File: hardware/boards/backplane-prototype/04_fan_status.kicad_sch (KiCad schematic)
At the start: 20 parts, among them J9 12V 3-WIRE FAN, Q1 AO3407A, Q2 2N7002

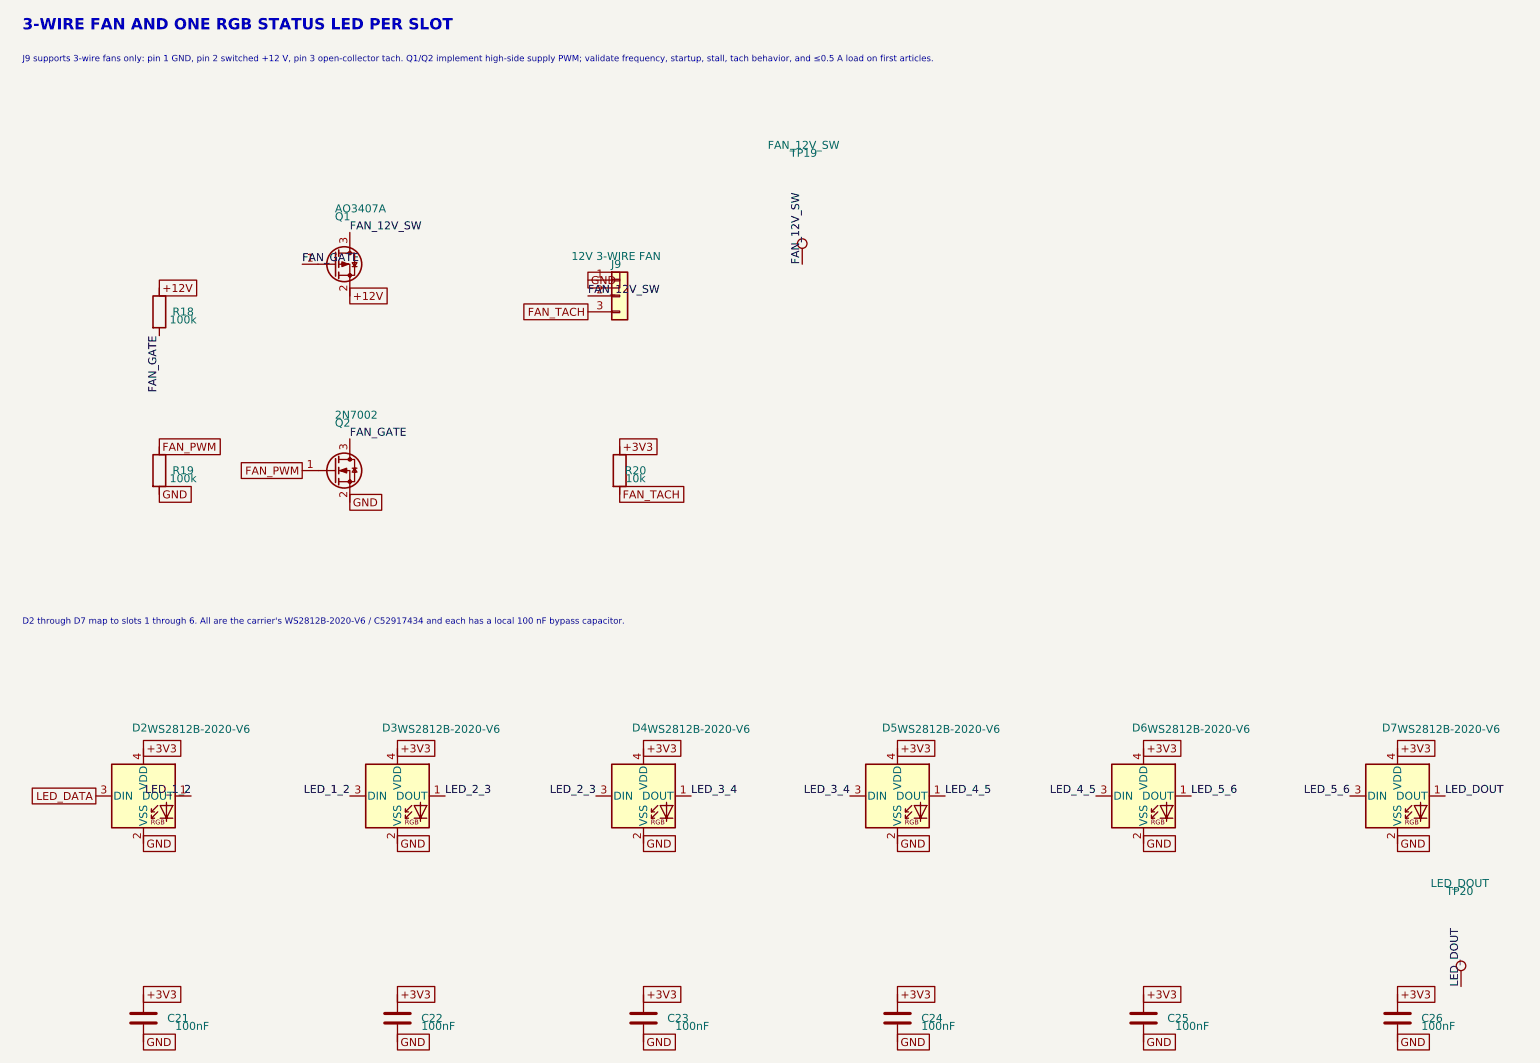
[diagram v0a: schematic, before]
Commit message: checkpoint backplane PCB synchronization
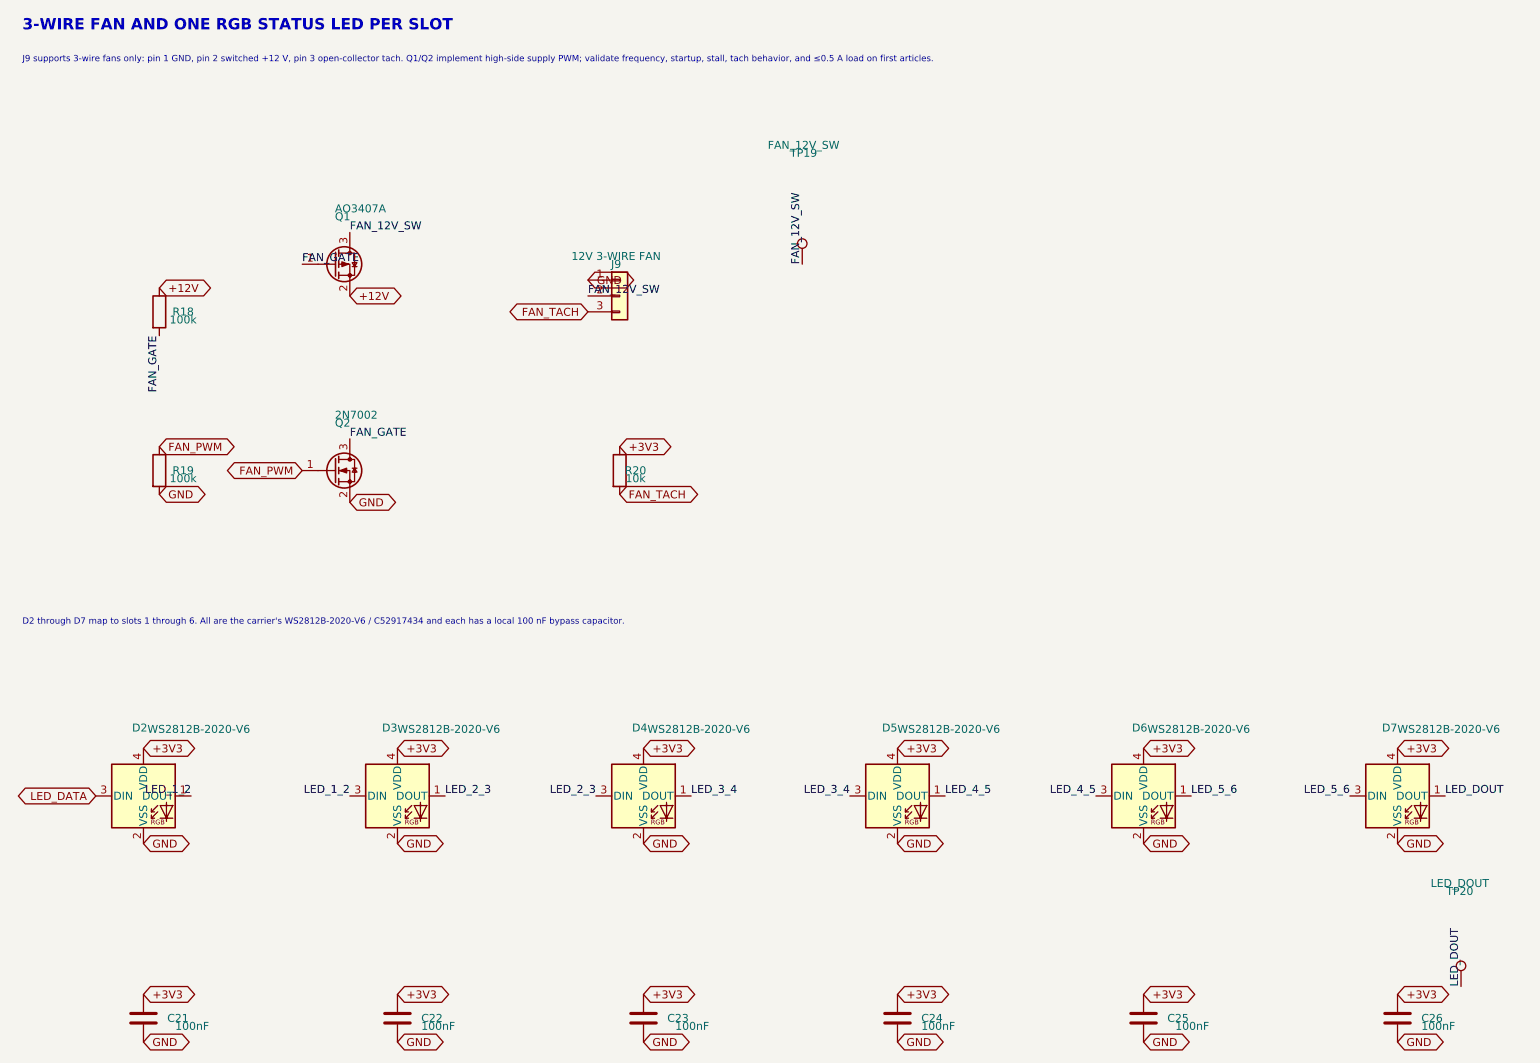
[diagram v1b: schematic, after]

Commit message: hardware: mark all test points DNP
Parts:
- TP19, TP20: now not fitted; now left out of the parts list
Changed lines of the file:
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@@
 		(body_style 1)
 		(exclude_from_sim no)
-		(in_bom yes)
+		(in_bom no)
 		(on_board yes)
 		(in_pos_files yes)
-		(dnp no)
+		(dnp yes)
 		(property "Reference" "TP20"
 			(at 250 154.94 0)
@@
 		(body_style 1)
 		(exclude_from_sim no)
-		(in_bom yes)
+		(in_bom no)
 		(on_board yes)
 		(in_pos_files yes)
-		(dnp no)
+		(dnp yes)
 		(property "Reference" "TP19"
 			(at 145 36.83 0)

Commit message: hardware: normalize C25803 BOM grouping
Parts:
- R18, R19: value 100k -> 100k 1%
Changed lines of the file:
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@@
 			)
 		)
-		(property "Value" "100k"
+		(property "Value" "100k 1%"
 			(at 45.72 63.5 0)
 			(show_name no)
@@
 			)
 		)
-		(property "Value" "100k"
+		(property "Value" "100k 1%"
 			(at 45.72 88.9 0)
 			(show_name no)

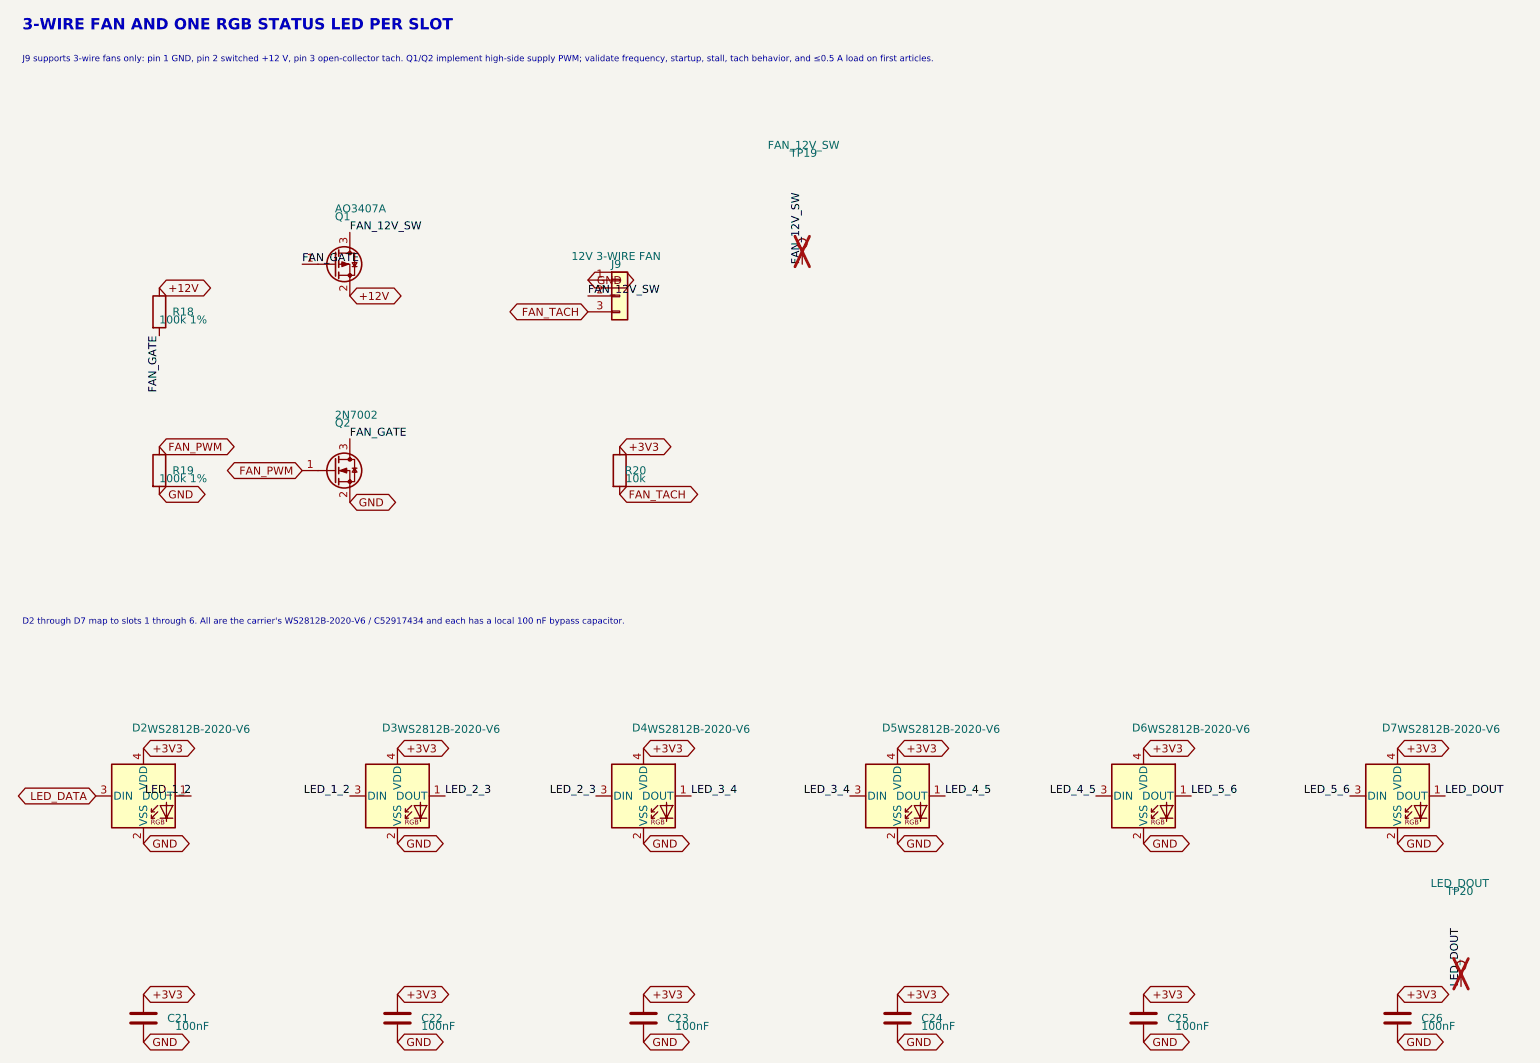
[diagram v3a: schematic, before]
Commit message: hardware: add backplane thermal interfaces
Add a second independent 3-wire fan channel and externally powered DS18B20 header, remove the slot NeoPixels, document the shared fan-rail limits, keep test points out of assembly exports, and move the four chassis holes to their nearest DRC-legal edge positions.
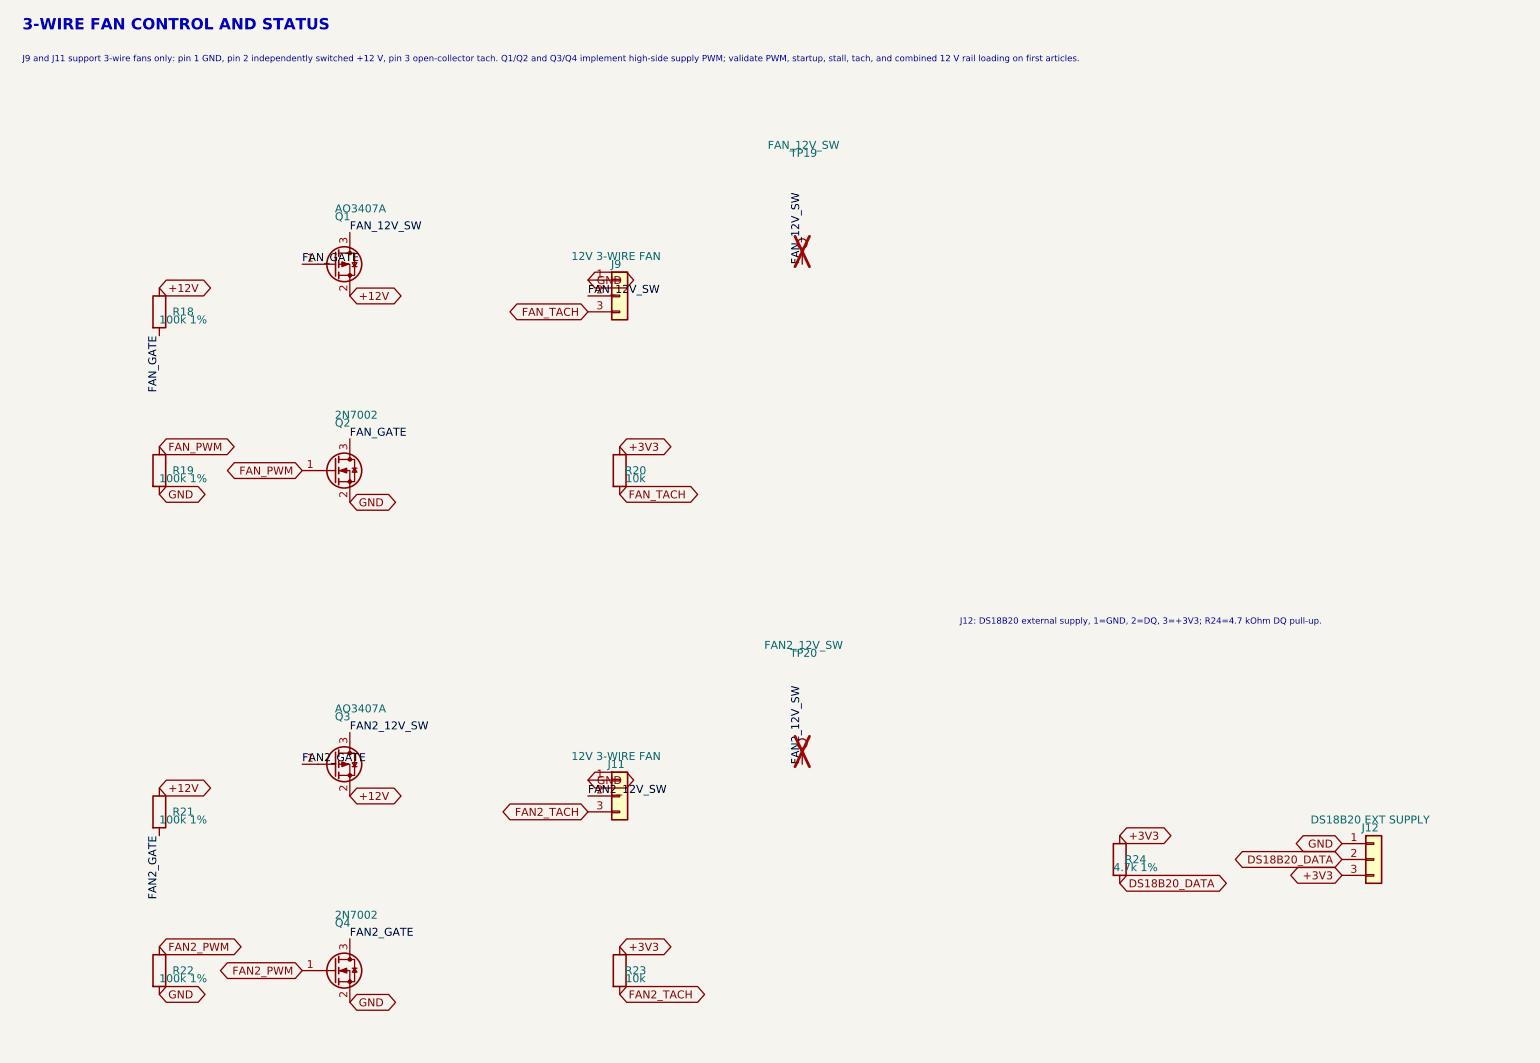
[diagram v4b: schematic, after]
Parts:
- removed C21, C22, C23, C24, C25, C26: 100nF, Capacitor_SMD:C_0603_1608Metric, symbol Device:C
- removed D2, D3, D4, D5, D6, D7: WS2812B-2020-V6, LED_SMD:LED_WS2812B-2020_PLCC4_2.0x2.0mm, symbol LED:WS2812B-2020
- added J11: 12V 3-WIRE FAN, Connector:FanPinHeader_1x03_P2.54mm_Vertical, symbol Connector_Generic:Conn_01x03
- added J12: DS18B20 EXT SUPPLY, Connector_PinHeader_2.54mm:PinHeader_1x03_P2.54mm_Vertical, symbol Connector_Generic:Conn_01x03
- added Q3: AO3407A, Package_TO_SOT_SMD:SOT-23, symbol Transistor_FET:Q_PMOS_GSD
- added Q4: 2N7002, Package_TO_SOT_SMD:SOT-23, symbol Transistor_FET:2N7002
- added R21, R22: 100k 1%, Resistor_SMD:R_0603_1608Metric, symbol Device:R
- added R23: 10k, Resistor_SMD:R_0603_1608Metric, symbol Device:R
- added R24: 4.7k 1%, Resistor_SMD:R_0603_1608Metric, symbol Device:R
- TP20: value LED_DOUT -> FAN2_12V_SW
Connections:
- net +12V: now also Q3.2 (S), R21.1
- net +3V3: now also J12.3 (Pin_3), R23.1, R24.1
- net GND: now also J11.1 (Pin_1), J12.1 (Pin_1), Q4.2 (S), R22.2
- net LED_DOUT renamed FAN2_12V_SW
- net FAN2_12V_SW: now also J11.2 (Pin_2), Q3.3 (D)
- new net DS18B20_DATA: J12.2 (Pin_2), R24.2
- new net FAN2_GATE: Q3.1 (G), Q4.3 (D), R21.2
- new net FAN2_PWM: Q4.1 (G), R22.1
- new net FAN2_TACH: J11.3 (Pin_3), R23.2
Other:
- note added: "3-WIRE FAN CONTROL AND STATUS"
- note added: "J12: DS18B20 external supply, 1=GND, 2=DQ, 3=+3V3; R24=4.7 kOhm DQ pull-up."
- note added: "J9 and J11 support 3-wire fans only: pin 1 GND, pin 2 independently switched +12 V, pin 3 open-collector tach. Q1/Q2 and Q3/Q4 implement high-side supply PWM; validate PWM, startup, stall, tach, and combined 12 V rail loading on first articles."
- note removed: "3-WIRE FAN AND ONE RGB STATUS LED PER SLOT"
- note removed: "D2 through D7 map to slots 1 through 6. All are the carrier's WS2812B-2020-V6 / C52917434 and each has a local 100 nF bypass capacitor."
- note removed: "J9 supports 3-wire fans only: pin 1 GND, pin 2 switched +12 V, pin 3 open-collector tach. Q1/Q2 implement high-side supply PWM; validate frequency, startup, stall, tach behavior, and ≤0.5 A load on first articles."

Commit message: hardware: align and lock fan connectors
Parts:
- J11, J9: footprint Connector:FanPinHeader_1x03_P2.54mm_Vertical -> Connector_MiniRackPower:FanPinHeader_1x03_P2.54mm_Vertical_JLC_Edge
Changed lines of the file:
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@@
 			)
 		)
-		(property "Footprint" "Connector:FanPinHeader_1x03_P2.54mm_Vertical"
+		(property "Footprint" "Connector_MiniRackPower:FanPinHeader_1x03_P2.54mm_Vertical_JLC_Edge"
 			(at 115 60 0)
 			(hide yes)
@@
 			)
 		)
-		(property "Footprint" "Connector:FanPinHeader_1x03_P2.54mm_Vertical"
+		(property "Footprint" "Connector_MiniRackPower:FanPinHeader_1x03_P2.54mm_Vertical_JLC_Edge"
 			(at 115 140.01 0)
 			(hide yes)

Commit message: checkpoint before LED1 3D model fix
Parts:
- removed TP19: FAN_12V_SW, TestPoint:TestPoint_Pad_D1.5mm, symbol Connector:TestPoint
- removed TP20: FAN2_12V_SW, TestPoint:TestPoint_Pad_D1.5mm, symbol Connector:TestPoint
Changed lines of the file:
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@@
-		)
-	)
-	(label "FAN2_12V_SW"
-		(at 144.78 134.62 90)
-		(effects
-			(font
-				(size 1.27 1.27)
-			)
-			(justify left bottom)
 		)
 	)
@@
 	(label "FAN2_GATE"
 		(at 64.77 134.62 0)
-		(effects
-			(font
-				(size 1.27 1.27)
-			)
-			(justify left bottom)
-		)
-	)
-	(label "FAN_12V_SW"
-		(at 144.78 54.61 90)
 		(effects
 			(font
@@
 	)
 	(symbol
-		(lib_id "Connector:TestPoint")
-		(at 144.78 134.62 0)
-		(unit 1)
-		(body_style 1)
-		(exclude_from_sim no)
-		(in_bom no)
-		(on_board yes)
-		(in_pos_files yes)
-		(dnp yes)
-		(property "Reference" "TP20"
-			(at 145 116.84 0)
-			(show_name no)
-			(do_not_autoplace no)
-			(effects
-				(font
-					(size 1.27 1.27)
-				)
-			)
-		)
-		(property "Value" "FAN2_12V_SW"
-			(at 145 115.57 0)
-			(show_name no)
-			(do_not_autoplace no)
-			(effects
-				(font
-					(size 1.27 1.27)
-				)
-			)
-		)
-		(property "Footprint" "TestPoint:TestPoint_Pad_D1.5mm"
-			(at 150.08 135.01 0)
-			(hide yes)
-			(show_name no)
-			(do_not_autoplace no)
-			(effects
-				(font
-					(size 1.27 1.27)
-				)
-			)
-		)
-		(property "Datasheet" ""
-			(at 150.08 135.01 0)
-			(hide yes)
-			(show_name no)
-			(do_not_autoplace no)
-			(effects
-				(font
-					(size 1.27 1.27)
-				)
-			)
-		)
-		(property "Description" "test point"
-			(at 145 135.01 0)
-			(hide yes)
-			(show_name no)
-			(do_not_autoplace no)
-			(effects
-				(font
-					(size 1.27 1.27)
-				)
-			)
-		)
-		(pin "1"
-		)
-		(instances
-			(project "backplane-prototype"
-				(path "/348cc909-6345-4013-9bef-98714057a65b/5d5cc60b-4c39-4882-898d-1aa7068798ee"
-					(reference "TP20")
-					(unit 1)
-				)
-			)
-		)
-	)
-	(symbol
 		(lib_id "Transistor_FET:Q_PMOS_GSD")
 		(at 69.85 54.61 0)
@@
 					(unit 1)
 				)
-			)
-		)
-	)
-	(symbol
-		(lib_id "Connector:TestPoint")
-		(at 144.78 54.61 0)
-		(unit 1)
-		(body_style 1)
-		(exclude_from_sim no)
-		(in_bom no)
-		(on_board yes)
-		(in_pos_files yes)
-		(dnp yes)
-		(property "Reference" "TP19"
-			(at 145 36.83 0)
-			(show_name no)
-			(do_not_autoplace no)
-			(effects
-				(font
-					(size 1.27 1.27)
-				)
-			)
-		)
-		(property "Value" "FAN_12V_SW"
-			(at 145 35.56 0)
-			(show_name no)
-			(do_not_autoplace no)
-			(effects
-				(font
-					(size 1.27 1.27)
-				)
-			)
-		)
-		(property "Footprint" "TestPoint:TestPoint_Pad_D1.5mm"
-			(at 150.08 55 0)
-			(hide yes)
-			(show_name no)
-			(do_not_autoplace no)
-			(effects
-				(font
-					(size 1.27 1.27)
-				)
-			)
-		)
-		(property "Datasheet" ""
-			(at 150.08 55 0)
-			(hide yes)
-			(show_name no)
-			(do_not_autoplace no)
-			(effects
-				(font
-					(size 1.27 1.27)
-				)
-			)
-		)
-		(property "Description" "test point"
-			(at 145 55 0)
-			(hide yes)
-			(show_name no)
-			(do_not_autoplace no)
-			(effects
-				(font
-					(size 1.27 1.27)
-				)
-			)
-		)
-		(pin "1"
-		)
-		(instances
-			(project "backplane-prototype"
-				(path "/348cc909-6345-4013-9bef-98714057a65b/5d5cc60b-4c39-4882-898d-1aa7068798ee"
-					(reference "TP19")
-					(unit 1)
-				)

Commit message: mark optional backplane headers DNP
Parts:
- J11, J12, J9: now not fitted
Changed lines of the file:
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@@
 		(on_board yes)
 		(in_pos_files yes)
-		(dnp no)
+		(dnp yes)
 		(property "Reference" "J11"
 			(at 115 134.62 0)
@@
 		(on_board yes)
 		(in_pos_files yes)
-		(dnp no)
+		(dnp yes)
 		(property "Reference" "J9"
 			(at 115 54.61 0)
@@
 		(on_board yes)
 		(in_pos_files yes)
-		(dnp no)
+		(dnp yes)
 		(property "Reference" "J12"
 			(at 235.65 144.78 0)
